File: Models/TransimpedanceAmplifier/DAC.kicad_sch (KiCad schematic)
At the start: 0 parts

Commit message: Filled in some detail
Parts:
- added U2: DAC81401PWR, PW0020A-IPC_A, symbol DAC81401:DAC81401PWR
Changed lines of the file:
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@@
 	(generator_version "9.0")
 	(paper "A4")
+	(symbol
+		(lib_id "DAC81401:DAC81401PWR")
+		(at 123.19 81.28 0)
+		(unit 1)
+		(exclude_from_sim no)
+		(in_bom yes)
+		(on_board yes)
+		(dnp no)
+		(fields_autoplaced yes)
+		(property "Reference" "U2"
+			(at 144.78 71.12 0)
+			(effects
+				(font
+					(size 1.524 1.524)
+				)
+			)
+		)
+		(property "Value" "DAC81401PWR"
+			(at 144.78 73.66 0)
+			(effects
+				(font
+					(size 1.524 1.524)
+				)
+			)
+		)
+		(property "Footprint" "PW0020A-IPC_A"
+			(at 123.19 81.28 0)
+			(effects
+				(font
+					(size 1.27 1.27)
+					(italic yes)
+				)
+				(hide yes)
+			)
+		)
+		(property "Datasheet" "https://www.ti.com/lit/gpn/dac81401"
+			(at 123.19 81.28 0)
+			(effects
+				(font
+					(size 1.27 1.27)
+					(italic yes)
+				)
+				(hide yes)
+			)
+		)
+		(property "Description" ""
+			(at 123.19 81.28 0)
+			(effects
+				(font
+					(size 1.27 1.27)
+				)
+				(hide yes)
+			)
+		)
+		(pin "13"
+		)
+		(pin "16"
+		)
+		(pin "7"
+		)
+		(pin "20"
+		)
+		(pin "9"
+		)
+		(pin "10"
+		)
+		(pin "11"
+		)
+		(pin "12"
+		)
+		(pin "4"
+		)
+		(pin "6"
+		)
+		(pin "8"
+		)
+		(pin "18"
+		)
+		(pin "2"
+		)
+		(pin "3"
+		)
+		(pin "19"
+		)
+		(pin "17"
+		)
+		(pin "1"
+		)
+		(pin "14"
+		)
+		(pin "15"
+		)
+		(pin "5"
+		)
+		(instances
+			(project ""
+				(path "/ec9f2ae3-e40d-40eb-9760-2b611ee8efd1/5646f584-34a2-41de-a9b6-e726812feaed"
+					(reference "U2")
+					(unit 1)
+				)
+			)
+		)
+	)
 )

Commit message: Save progress
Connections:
- net 3.3V: now reaches U2.17 (IOVDD)
- net GND: now reaches U2.19 (DVSS)
- net GND: now also U2.2 (VREFGND)
- net 5V: now reaches U2.20 (DVDD)
- net -15V: now reaches U2.3 (AVSS)
- net 15V: now reaches U2.5 (AVDD)
- no-connect marks 0 -> 4
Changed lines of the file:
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@@
 	(generator_version "9.0")
 	(paper "A4")
+	(no_connect
+		(at 167.64 104.14)
+	)
+	(no_connect
+		(at 167.64 106.68)
+	)
+	(no_connect
+		(at 167.64 99.06)
+	)
+	(no_connect
+		(at 167.64 101.6)
+	)
+	(wire
+		(pts
+			(xy 167.64 116.84) (xy 175.26 116.84)
+		)
+		(stroke
+			(width 0)
+			(type default)
+		)
+	)
+	(wire
+		(pts
+			(xy 175.26 116.84) (xy 175.26 119.38)
+		)
+		(stroke
+			(width 0)
+			(type default)
+		)
+	)
+	(wire
+		(pts
+			(xy 175.26 109.22) (xy 175.26 111.76)
+		)
+		(stroke
+			(width 0)
+			(type default)
+		)
+	)
+	(wire
+		(pts
+			(xy 167.64 111.76) (xy 175.26 111.76)
+		)
+		(stroke
+			(width 0)
+			(type default)
+		)
+	)
+	(hierarchical_label "5V"
+		(shape input)
+		(at 121.92 83.82 180)
+		(effects
+			(font
+				(size 1.27 1.27)
+			)
+			(justify right)
+		)
+	)
+	(hierarchical_label "3.3V"
+		(shape input)
+		(at 121.92 86.36 180)
+		(effects
+			(font
+				(size 1.27 1.27)
+			)
+			(justify right)
+		)
+	)
+	(hierarchical_label "15V"
+		(shape input)
+		(at 121.92 81.28 180)
+		(effects
+			(font
+				(size 1.27 1.27)
+			)
+			(justify right)
+		)
+	)
+	(hierarchical_label "-15V"
+		(shape input)
+		(at 167.64 114.3 0)
+		(effects
+			(font
+				(size 1.27 1.27)
+			)
+			(justify left)
+		)
+	)
+	(symbol
+		(lib_id "power:GND")
+		(at 175.26 119.38 0)
+		(unit 1)
+		(exclude_from_sim no)
+		(in_bom yes)
+		(on_board yes)
+		(dnp no)
+		(fields_autoplaced yes)
+		(property "Reference" "#PWR07"
+			(at 175.26 125.73 0)
+			(effects
+				(font
+					(size 1.27 1.27)
+				)
+				(hide yes)
+			)
+		)
+		(property "Value" "GND"
+			(at 175.26 124.46 0)
+			(effects
+				(font
+					(size 1.27 1.27)
+				)
+			)
+		)
+		(property "Footprint" ""
+			(at 175.26 119.38 0)
+			(effects
+				(font
+					(size 1.27 1.27)
+				)
+				(hide yes)
+			)
+		)
+		(property "Datasheet" ""
+			(at 175.26 119.38 0)
+			(effects
+				(font
+					(size 1.27 1.27)
+				)
+				(hide yes)
+			)
+		)
+		(property "Description" "Power symbol creates a global label with name \"GND\" , ground"
+			(at 175.26 119.38 0)
+			(effects
+				(font
+					(size 1.27 1.27)
+				)
+				(hide yes)
+			)
+		)
+		(pin "1"
+		)
+		(instances
+			(project ""
+				(path "/ec9f2ae3-e40d-40eb-9760-2b611ee8efd1/5646f584-34a2-41de-a9b6-e726812feaed"
+					(reference "#PWR07")
+					(unit 1)
+				)
+			)
+		)
+	)
+	(symbol
+		(lib_id "power:GND")
+		(at 175.26 109.22 180)
+		(unit 1)
+		(exclude_from_sim no)
+		(in_bom yes)
+		(on_board yes)
+		(dnp no)
+		(fields_autoplaced yes)
+		(property "Reference" "#PWR08"
+			(at 175.26 102.87 0)
+			(effects
+				(font
+					(size 1.27 1.27)
+				)
+				(hide yes)
+			)
+		)
+		(property "Value" "GND"
+			(at 175.26 104.14 0)
+			(effects
+				(font
+					(size 1.27 1.27)
+				)
+			)
+		)
+		(property "Footprint" ""
+			(at 175.26 109.22 0)
+			(effects
+				(font
+					(size 1.27 1.27)
+				)
+				(hide yes)
+			)
+		)
+		(property "Datasheet" ""
+			(at 175.26 109.22 0)
+			(effects
+				(font
+					(size 1.27 1.27)
+				)
+				(hide yes)
+			)
+		)
+		(property "Description" "Power symbol creates a global label with name \"GND\" , ground"
+			(at 175.26 109.22 0)
+			(effects
+				(font
+					(size 1.27 1.27)
+				)
+				(hide yes)
+			)
+		)
+		(pin "1"
+		)
+		(instances
+			(project ""
+				(path "/ec9f2ae3-e40d-40eb-9760-2b611ee8efd1/5646f584-34a2-41de-a9b6-e726812feaed"
+					(reference "#PWR08")
+					(unit 1)
+				)
+			)
+		)
+	)
 	(symbol
 		(lib_id "DAC81401:DAC81401PWR")

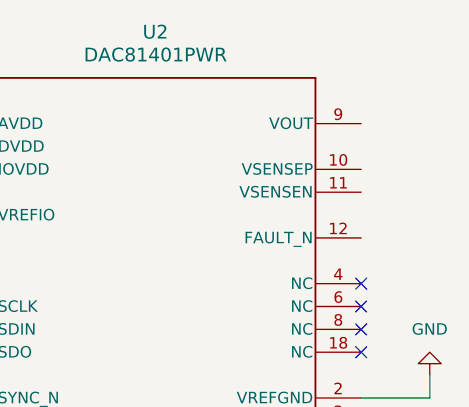
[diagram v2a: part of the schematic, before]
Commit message: Specified the power I/O sheet pins for the ADC
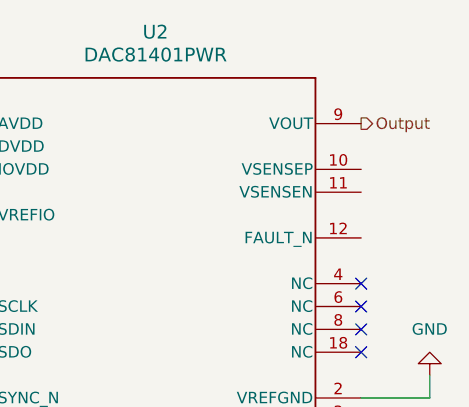
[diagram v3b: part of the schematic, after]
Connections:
- net Output: now reaches U2.9 (VOUT)
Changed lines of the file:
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@@
+		)
+	)
+	(hierarchical_label "Output"
+		(shape output)
+		(at 167.64 81.28 0)
+		(effects
+			(font
+				(size 1.27 1.27)
+			)
+			(justify left)
 		)
 	)

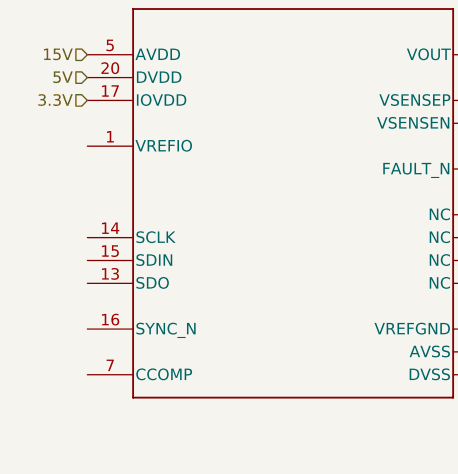
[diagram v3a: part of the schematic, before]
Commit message: Assigned all the SPI pins
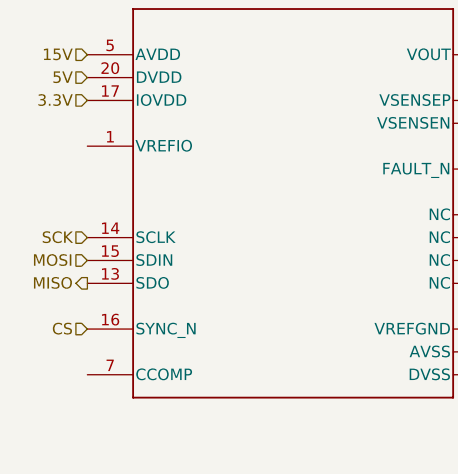
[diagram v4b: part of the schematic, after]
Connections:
- net MISO: now reaches U2.13 (SDO)
- net SCK: now reaches U2.14 (SCLK)
- net MOSI: now reaches U2.15 (SDIN)
- net CS: now reaches U2.16 (SYNC_N)
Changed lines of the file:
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@@
+		)
+	)
+	(hierarchical_label "MISO"
+		(shape output)
+		(at 121.92 106.68 180)
+		(effects
+			(font
+				(size 1.27 1.27)
+			)
+			(justify right)
 		)
 	)
@@
 		(shape input)
 		(at 121.92 83.82 180)
+		(effects
+			(font
+				(size 1.27 1.27)
+			)
+			(justify right)
+		)
+	)
+	(hierarchical_label "MOSI"
+		(shape input)
+		(at 121.92 104.14 180)
+		(effects
+			(font
+				(size 1.27 1.27)
+			)
+			(justify right)
+		)
+	)
+	(hierarchical_label "SCK"
+		(shape input)
+		(at 121.92 101.6 180)
 		(effects
 			(font
@@
 		(effects
 			(font
+				(size 1.27 1.27)
+			)
+			(justify right)
+		)
+	)
+	(hierarchical_label "CS"
+		(shape input)
+		(at 121.92 111.76 180)
+		(effects
+			(font

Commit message: All suppliers are out of stock of LM7915L in the simple TO-92-3 package. Resolve this by first tabulating the maximum possible current on each regulator.
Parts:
- U2: Purchase Link (none) -> https://www.digikey.com/en/products/detail/texas-instrument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
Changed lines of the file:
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@@
+			)
+		)
+		(property "Purchase Link" "https://www.digikey.com/en/products/detail/texas-instruments/DAC81401PWR/22077523"
+			(at 123.19 81.28 0)
+			(effects
+				(font
+					(size 1.27 1.27)
+				)
+				(hide yes)
 			)
 		)

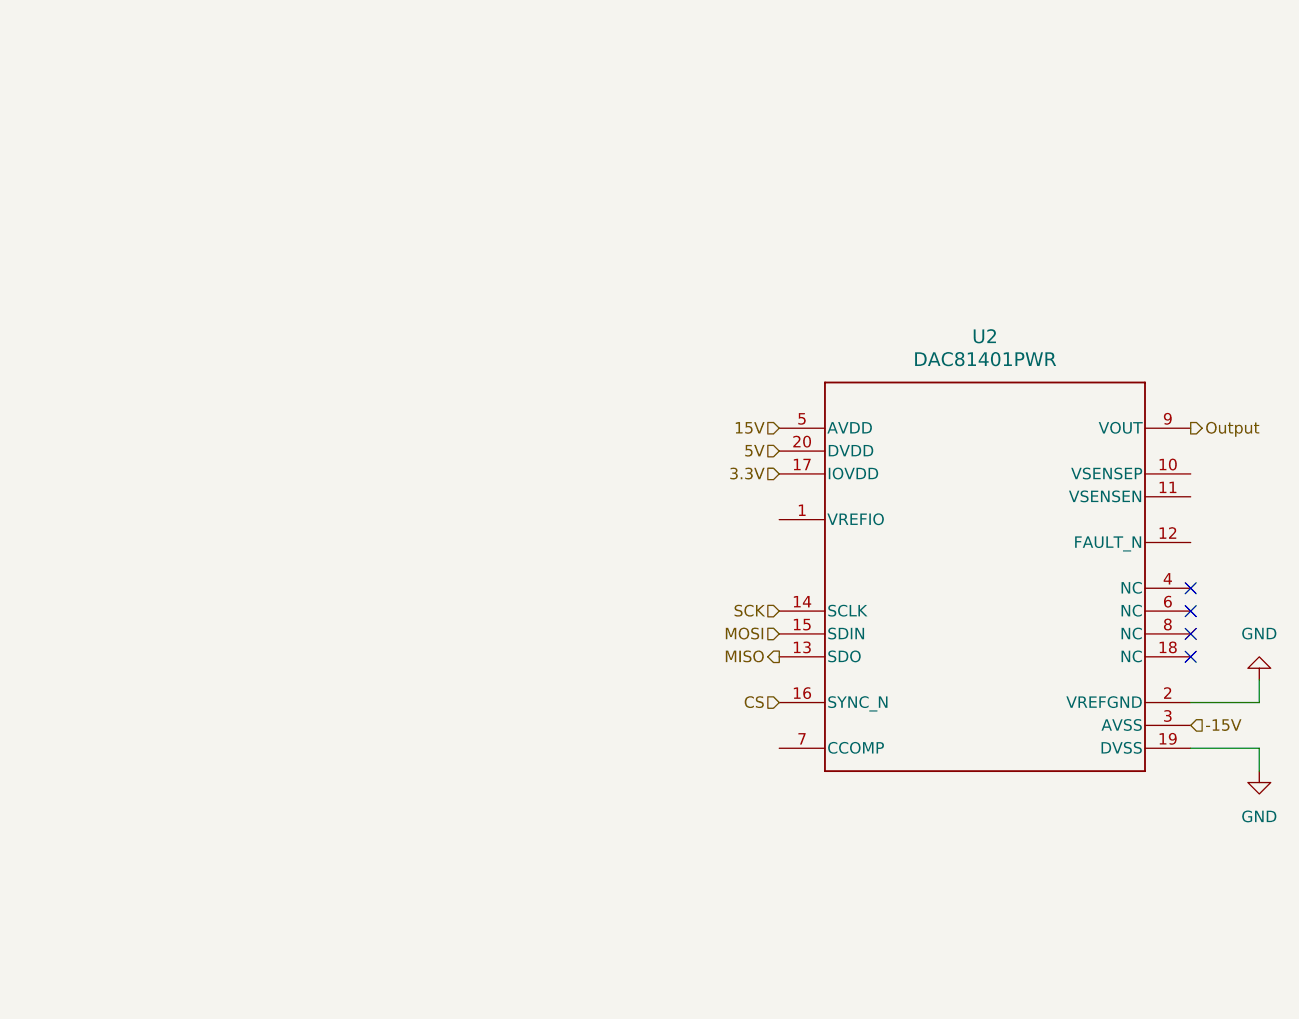
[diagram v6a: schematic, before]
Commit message: Finished writing the ADC's network
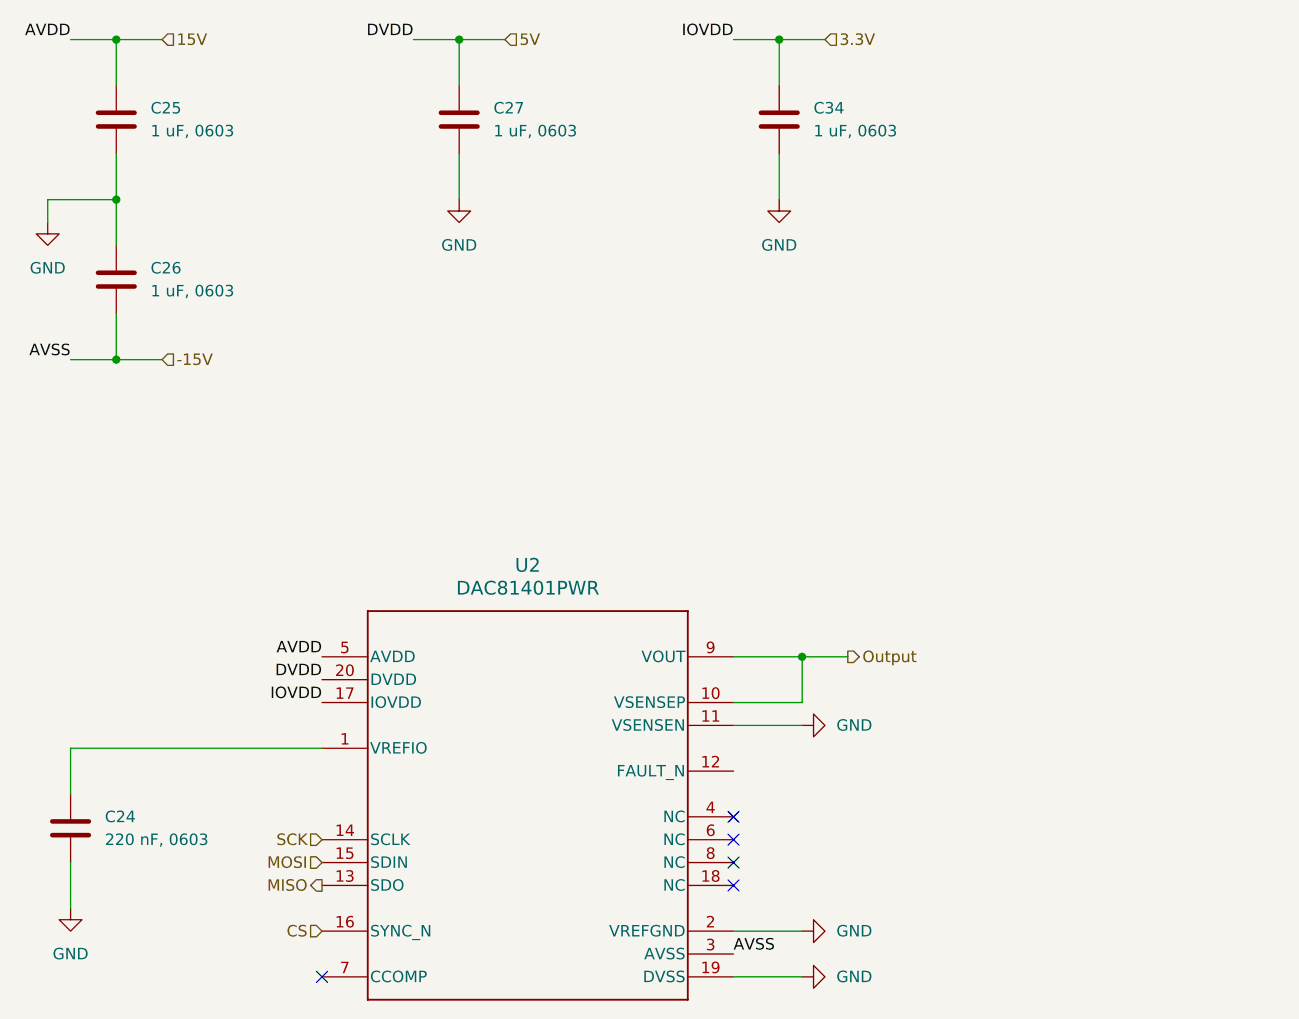
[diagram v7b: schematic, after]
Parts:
- added C24: 220 nF, 0603, symbol Device:C
- added C25, C26, C27, C34: 1 uF, 0603, symbol Device:C
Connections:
- net -15V: now also C26.2
- net 15V: now also C25.1
- net 3.3V: now also C34.1
- net 5V: now also C27.1
- net GND: now also U2.11 (VSENSEN), C24.2, C25.2, C26.1, C27.2, C34.2
- net Output: now also U2.10 (VSENSEP)
- net at U2.1 (VREFIO): now also C24.1
- no-connect marks 4 -> 5
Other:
- moved on the sheet: U2

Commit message: Finished for today
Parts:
- C24, C25, C26, C27, C34: Purchase Link (none) -> https://www.digikey.com/en/products/detail/murata-electroni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
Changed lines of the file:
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@@
 			)
 		)
-		(property "Purchase Link" ""
+		(property "Purchase Link" "https://www.digikey.com/en/products/detail/murata-electronics/GRT188R61H105KE13D/5416752"
 			(at 48.26 46.99 0)
 			(effects
@@
 			)
 		)
-		(property "Purchase Link" ""
+		(property "Purchase Link" "https://www.digikey.com/en/products/detail/murata-electronics/GRT188R61H105KE13D/5416752"
 			(at 121.92 46.99 0)
 			(effects
@@
 			)
 		)
-		(property "Purchase Link" ""
+		(property "Purchase Link" "https://www.digikey.com/en/products/detail/murata-electronics/GRT188R61H105KE13D/5416752"
 			(at 86.36 46.99 0)
 			(effects
@@
 			)
 		)
+		(property "Purchase Link" "https://www.digikey.com/en/products/detail/murata-electronics/GRM188R71H224KAC4D/5797498"
+			(at 43.18 125.73 0)
+			(effects
+				(font
+					(size 1.27 1.27)
+				)
+				(hide yes)
+			)
+		)
 		(pin "2"
 		)
@@
 			(at 48.26 64.77 0)
 			(effects
+				(font
+					(size 1.27 1.27)
+				)
+				(hide yes)
+			)
+		)
+		(property "Purchase Link" "https://www.digikey.com/en/products/detail/murata-electronics/GRT188R61H105KE13D/5416752"
+			(at 48.26 64.77 0)
+			(effects
